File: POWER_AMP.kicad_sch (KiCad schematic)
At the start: 6 parts, among them U13 SE5023L-R

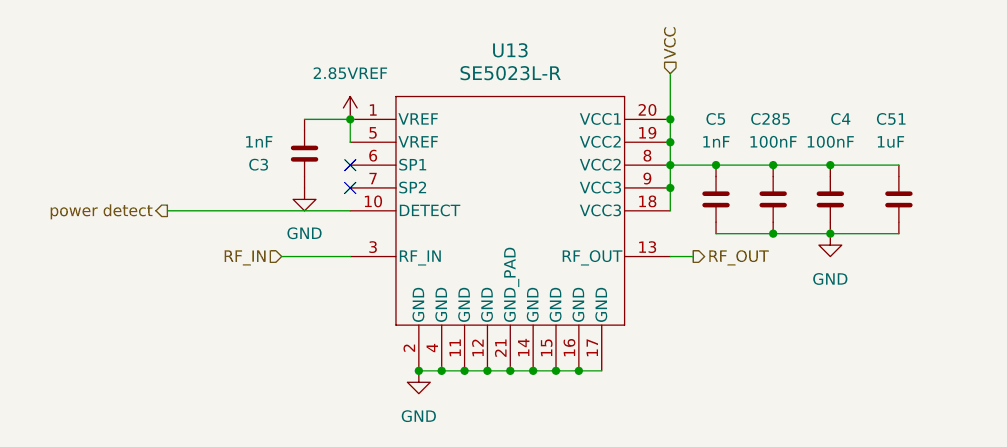
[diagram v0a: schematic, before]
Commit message: created fab files, needs some cleanup
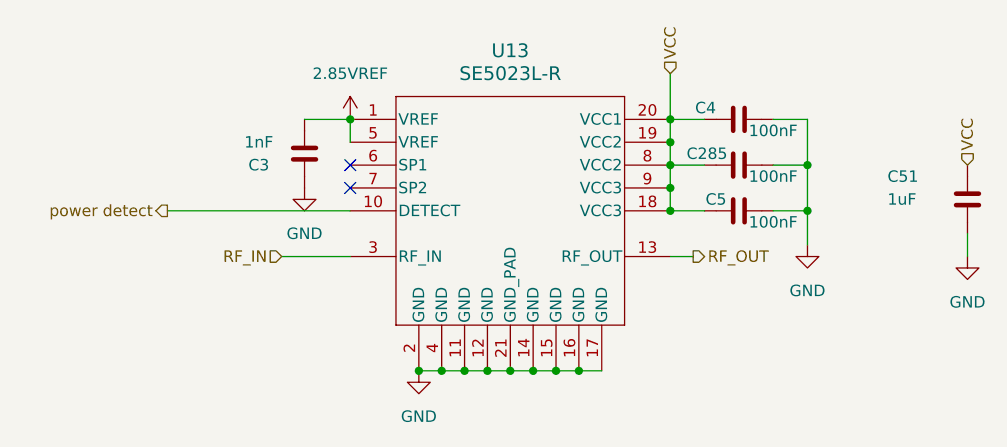
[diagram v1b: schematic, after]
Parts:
- C5: value 1nF -> 100nF; symbol Capacitors:0402_nF1_50V -> Capacitors:0402_nF100_50V; DN 490-GCM1555C1H102GA16JCT-ND -> 490-14514-1-ND; MFR (none) -> Murata Electronics; MPN GCM1555C1H102GA16J -> GCM155R71H104KE02J; price .07 -> .02
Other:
- moved on the sheet: C5, C51

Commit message: updated bom
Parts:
- U13: DN 863-SE5023L-RCT-ND -> 863-1376-1-ND; MPN SE5023L-R -> 5004L-R
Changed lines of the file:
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@@
 			)
 		)
-		(property "Description" "8.15-1.85GHz power amp"
+		(property "Description" "8.15-1.85GHz power amp substitute: 5004L-R"
 			(at 71.374 47.498 0)
 			(hide yes)
@@
 			)
 		)
-		(property "MPN" "SE5023L-R"
+		(property "MPN" "5004L-R"
 			(at 64.008 51.562 0)
 			(hide yes)
@@
 			)
 		)
-		(property "DN" "863-SE5023L-RCT-ND"
+		(property "DN" "863-1376-1-ND"
 			(at 71.374 47.498 0)
 			(hide yes)
